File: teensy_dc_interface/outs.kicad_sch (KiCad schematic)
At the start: 92 parts, among them J1 3.5mm_Mono_Switched_SymSmall_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, J2 3.5mm_Mono_Switched_SymSmall_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, J3 3.5mm_Mono_Switched_SymSmall_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, J4 3.5mm_Mono_Switched_SymSmall_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, J5 3.5mm_Mono_Switched_SymSmall_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, J6 3.5mm_Mono_Switched_SymSmall_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, J7 3.5mm_Mono_Switched_SymSmall_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, J8 3.5mm_Mono_Switched_SymSmall_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, U5 NE5532, U6 NE5532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

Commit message: teensy to dac connections
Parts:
- TP1, TP2, TP3, TP4, TP5, TP6, TP7, TP8: footprint (none) -> TestPoint:TestPoint_Keystone_5005-5009_Compact
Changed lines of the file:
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@@
 			)
 		)
-		(property "Footprint" ""
+		(property "Footprint" "TestPoint:TestPoint_Keystone_5005-5009_Compact"
 			(at 156.21 149.86 0)
 			(effects
@@
 			)
 		)
-		(property "Footprint" ""
+		(property "Footprint" "TestPoint:TestPoint_Keystone_5005-5009_Compact"
 			(at 156.21 106.68 0)
 			(effects
@@
 			)
 		)
-		(property "Footprint" ""
+		(property "Footprint" "TestPoint:TestPoint_Keystone_5005-5009_Compact"
 			(at 80.01 106.68 0)
 			(effects
@@
 			)
 		)
-		(property "Footprint" ""
+		(property "Footprint" "TestPoint:TestPoint_Keystone_5005-5009_Compact"
 			(at 156.21 20.32 0)
 			(effects
@@
 			)
 		)
-		(property "Footprint" ""
+		(property "Footprint" "TestPoint:TestPoint_Keystone_5005-5009_Compact"
 			(at 80.01 149.86 0)
 			(effects
@@
 			)
 		)
-		(property "Footprint" ""
+		(property "Footprint" "TestPoint:TestPoint_Keystone_5005-5009_Compact"
 			(at 80.01 63.5 0)
 			(effects
@@
 			)
 		)
-		(property "Footprint" ""
+		(property "Footprint" "TestPoint:TestPoint_Keystone_5005-5009_Compact"
 			(at 156.21 63.5 0)
 			(effects
@@
 			)
 		)
-		(property "Footprint" ""
+		(property "Footprint" "TestPoint:TestPoint_Keystone_5005-5009_Compact"
 			(at 80.01 20.32 0)
 			(effects

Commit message: Updated filtering between VREF's. Added separate power supply for Teensy on 5V. Added test points. Added ADC input
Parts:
- added J12, J13: 3.5mm_Mono_Switched_SymSmall_0.05, 4ms_Jack:EighthInch_PJ398SM, symbol PCM_4ms_Jack:3.5mm_Mono_Switched_SymSmall_0.05
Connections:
- net GNDA: now also J12.2 (SHEILD), J12.3 (SW), J13.2 (SHEILD), J13.3 (SW)
- new net ADC2: J12.1 (SIG)
- new net ADC3: J13.1 (SIG)

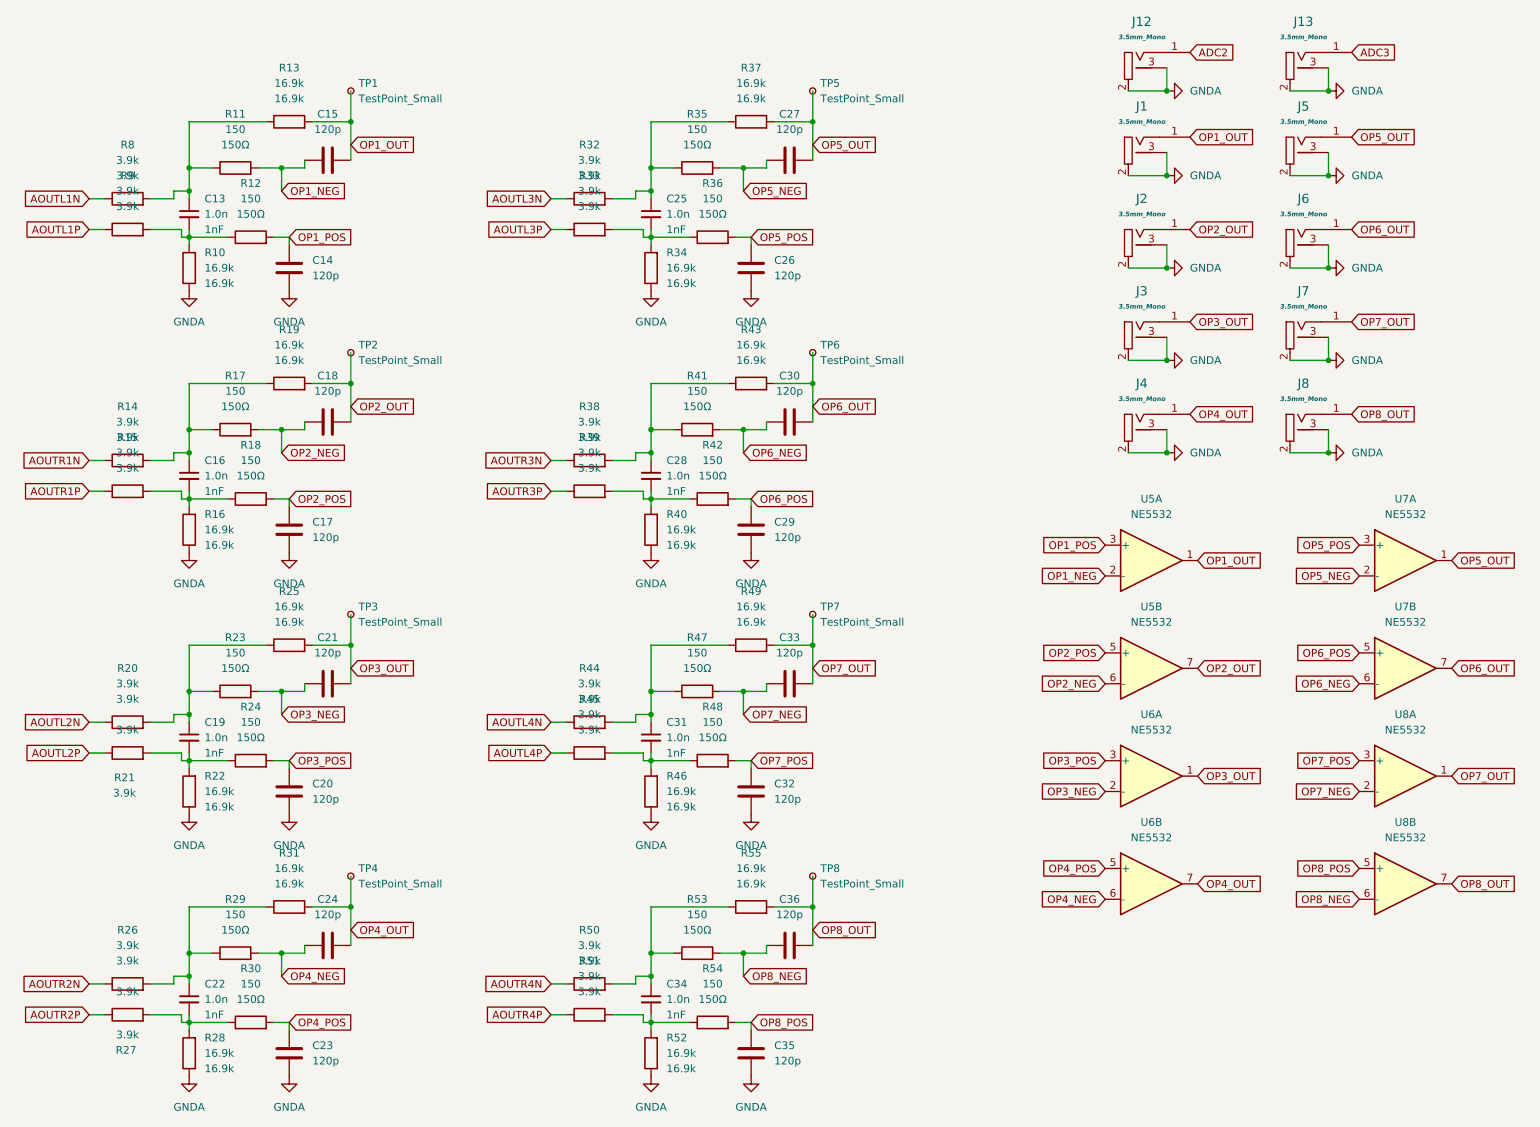
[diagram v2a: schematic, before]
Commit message: out pairs as pages
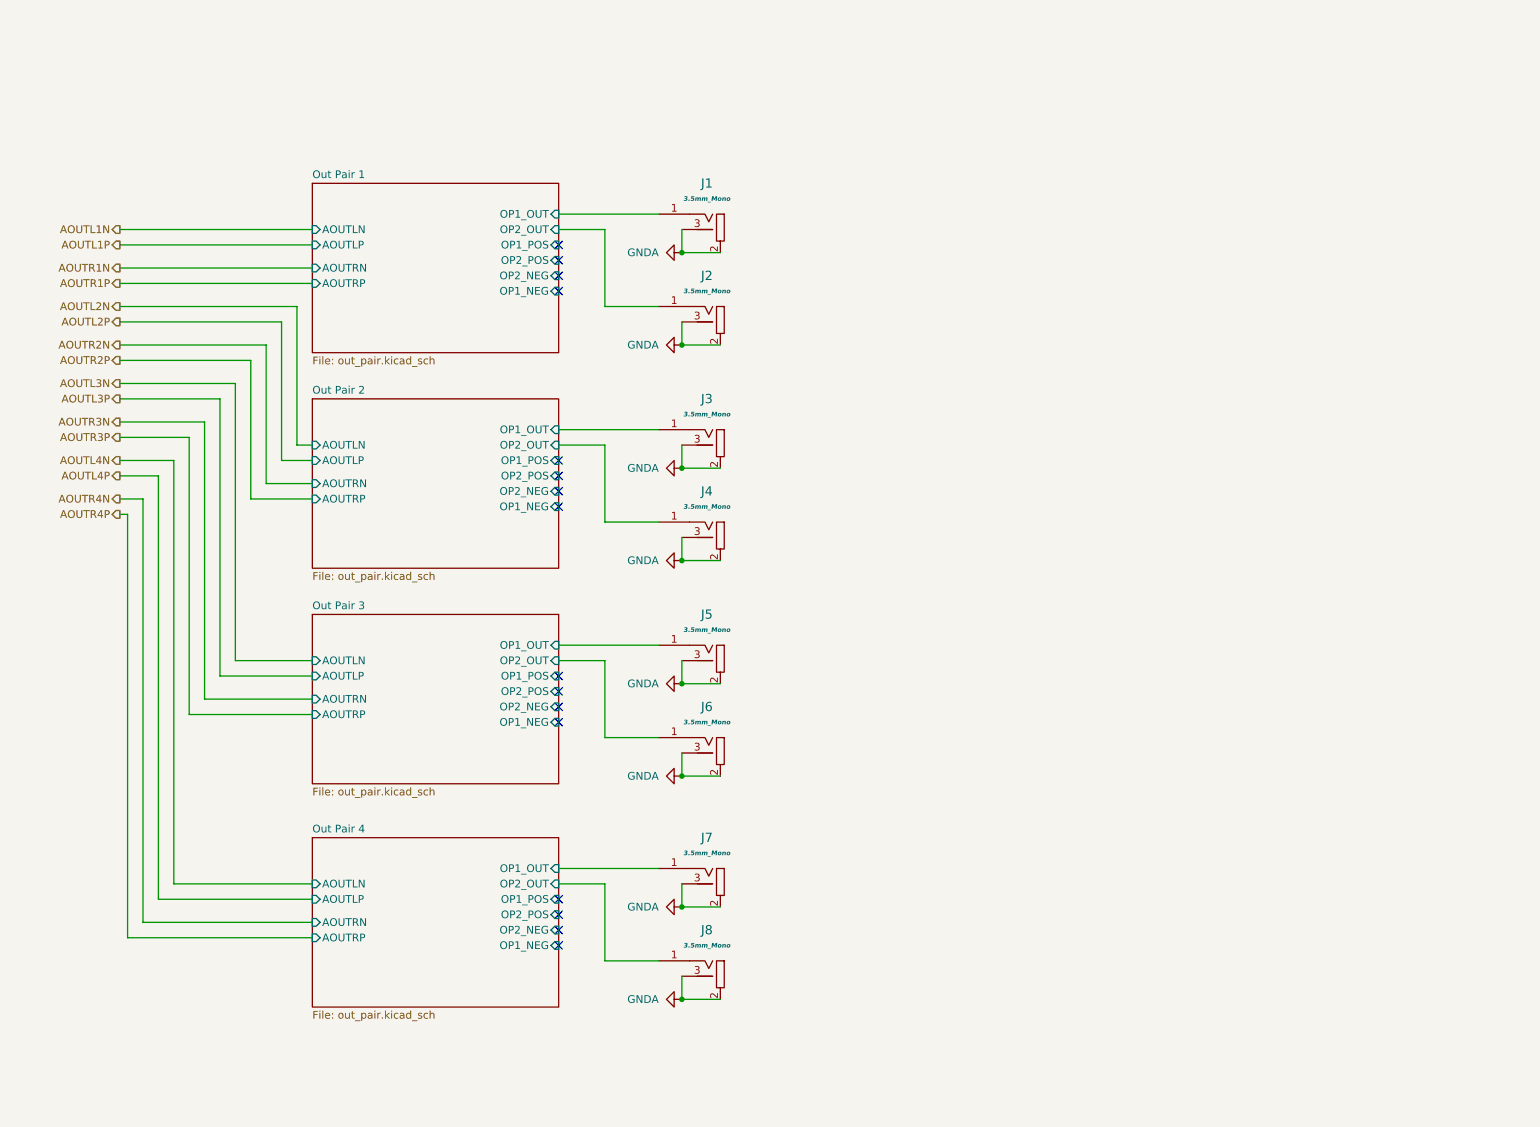
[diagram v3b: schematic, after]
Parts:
- removed C13, C16, C19, C22, C25, C28, C31, C34: 1.0n, 4ms_Capacitor:C_0402, symbol 4ms_Capacitor:1nF_0402_50V
- removed C14, C15, C17, C18, C20, C21, C23, C24, C26, C27, C29, C30, C32, C33, C35, C36: 120p, 4ms_Capacitor:C_0402, symbol Device:C
- removed J12, J13: 3.5mm_Mono_Switched_SymSmall_0.05, 4ms_Jack:EighthInch_PJ398SM, symbol PCM_4ms_Jack:3.5mm_Mono_Switched_SymSmall_0.05
- removed R10, R13, R16, R19, R22, R25, R28, R31, R34, R37, R40, R43, R46, R49, R52, R55: 16.9k, 4ms_Resistor:R_0402, symbol 4ms_Resistor_0402:16.9k_0402
- removed R11, R12, R17, R18, R23, R24, R29, R30, R35, R36, R41, R42, R47, R48, R53, R54: 150, 4ms_Resistor:R_0402, symbol 4ms_Resistor_0402:150Ω_0402
- removed R14, R15, R20, R21, R26, R27, R32, R33, R38, R39, R44, R45, R50, R51, R8, R9: 3.9k, 4ms_Resistor:R_0402, symbol 4ms_Resistor_0402:3.9k_0402
- removed TP1, TP2, TP3, TP4, TP5, TP6, TP7, TP8: TestPoint_Small, TestPoint:TestPoint_Keystone_5005-5009_Compact, symbol 4ms_Connector:TestPoint_Small
- removed U5, U6, U7, U8: NE5532, NE5532DR:SOIC127P599X175-8N, symbol Amplifier_Operational:NE5532
- J1: value 3.5mm_Mono_Switched_SymSmall_0.05 -> Chan 1 Out
- J2: value 3.5mm_Mono_Switched_SymSmall_0.05 -> Chan 2 Out
- J3: value 3.5mm_Mono_Switched_SymSmall_0.05 -> Chan 3 Out
- J4: value 3.5mm_Mono_Switched_SymSmall_0.05 -> Chan 4 Out
- J5: value 3.5mm_Mono_Switched_SymSmall_0.05 -> Chan 5 Out
- J6: value 3.5mm_Mono_Switched_SymSmall_0.05 -> Chan 6 Out
- J7: value 3.5mm_Mono_Switched_SymSmall_0.05 -> Chan 7 Out
- J8: value 3.5mm_Mono_Switched_SymSmall_0.05 -> Chan 8 Out
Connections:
- net OP1_OUT renamed Out Pair 1/OP1_OUT
- net OP2_OUT renamed Out Pair 1/OP2_OUT
- net OP3_OUT renamed Out Pair 2/OP1_OUT
- net OP4_OUT renamed Out Pair 2/OP2_OUT
- net OP5_OUT renamed Out Pair 3/OP1_OUT
- net OP6_OUT renamed Out Pair 3/OP2_OUT
- net OP7_OUT renamed Out Pair 4/OP1_OUT
- net OP8_OUT renamed Out Pair 4/OP2_OUT
- no-connect marks 0 -> 16
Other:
- added sheet Out Pair 1 (out_pair.kicad_sch)
- added sheet Out Pair 2 (out_pair.kicad_sch)
- added sheet Out Pair 3 (out_pair.kicad_sch)
- added sheet Out Pair 4 (out_pair.kicad_sch)
